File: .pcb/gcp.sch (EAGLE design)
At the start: 14 parts, among them SW1 POWER/COFFEE_SWITCHON-OFF

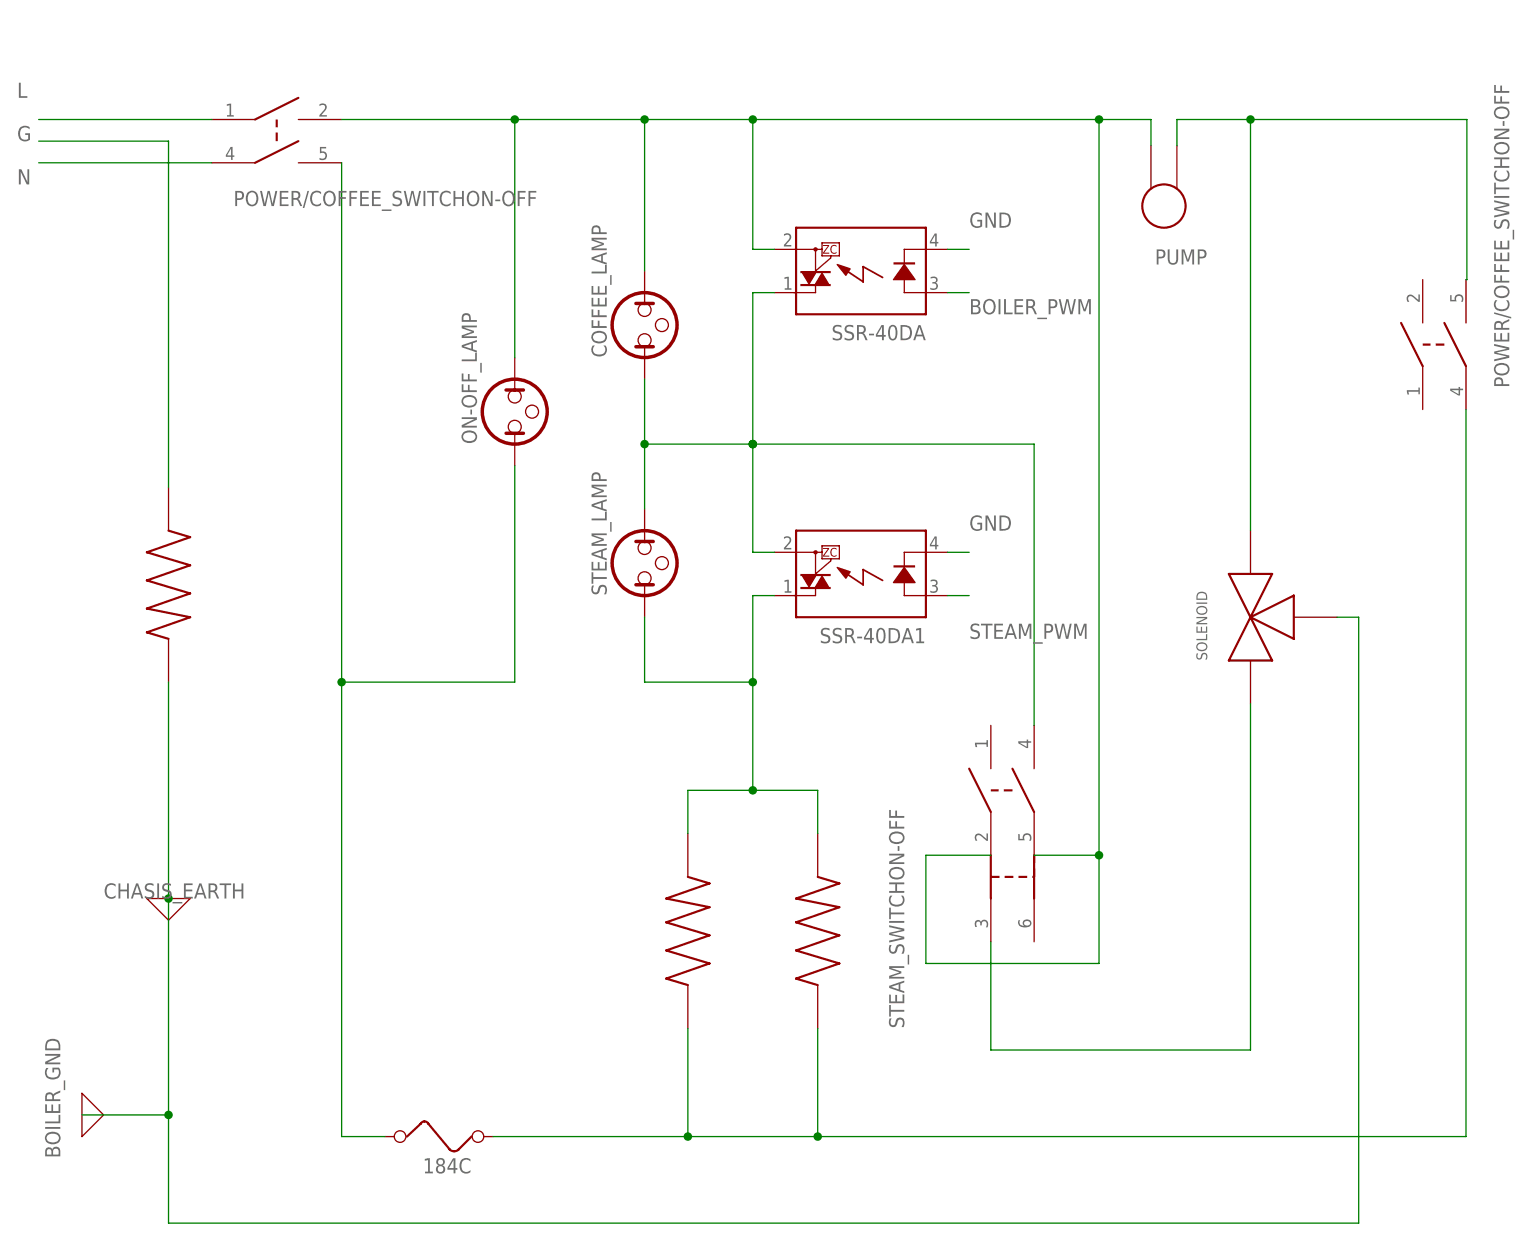
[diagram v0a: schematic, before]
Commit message: Remove references to lights and switches. Updated sketch to reflect how wiring of relays will work (lights will be controlled via physical logic)
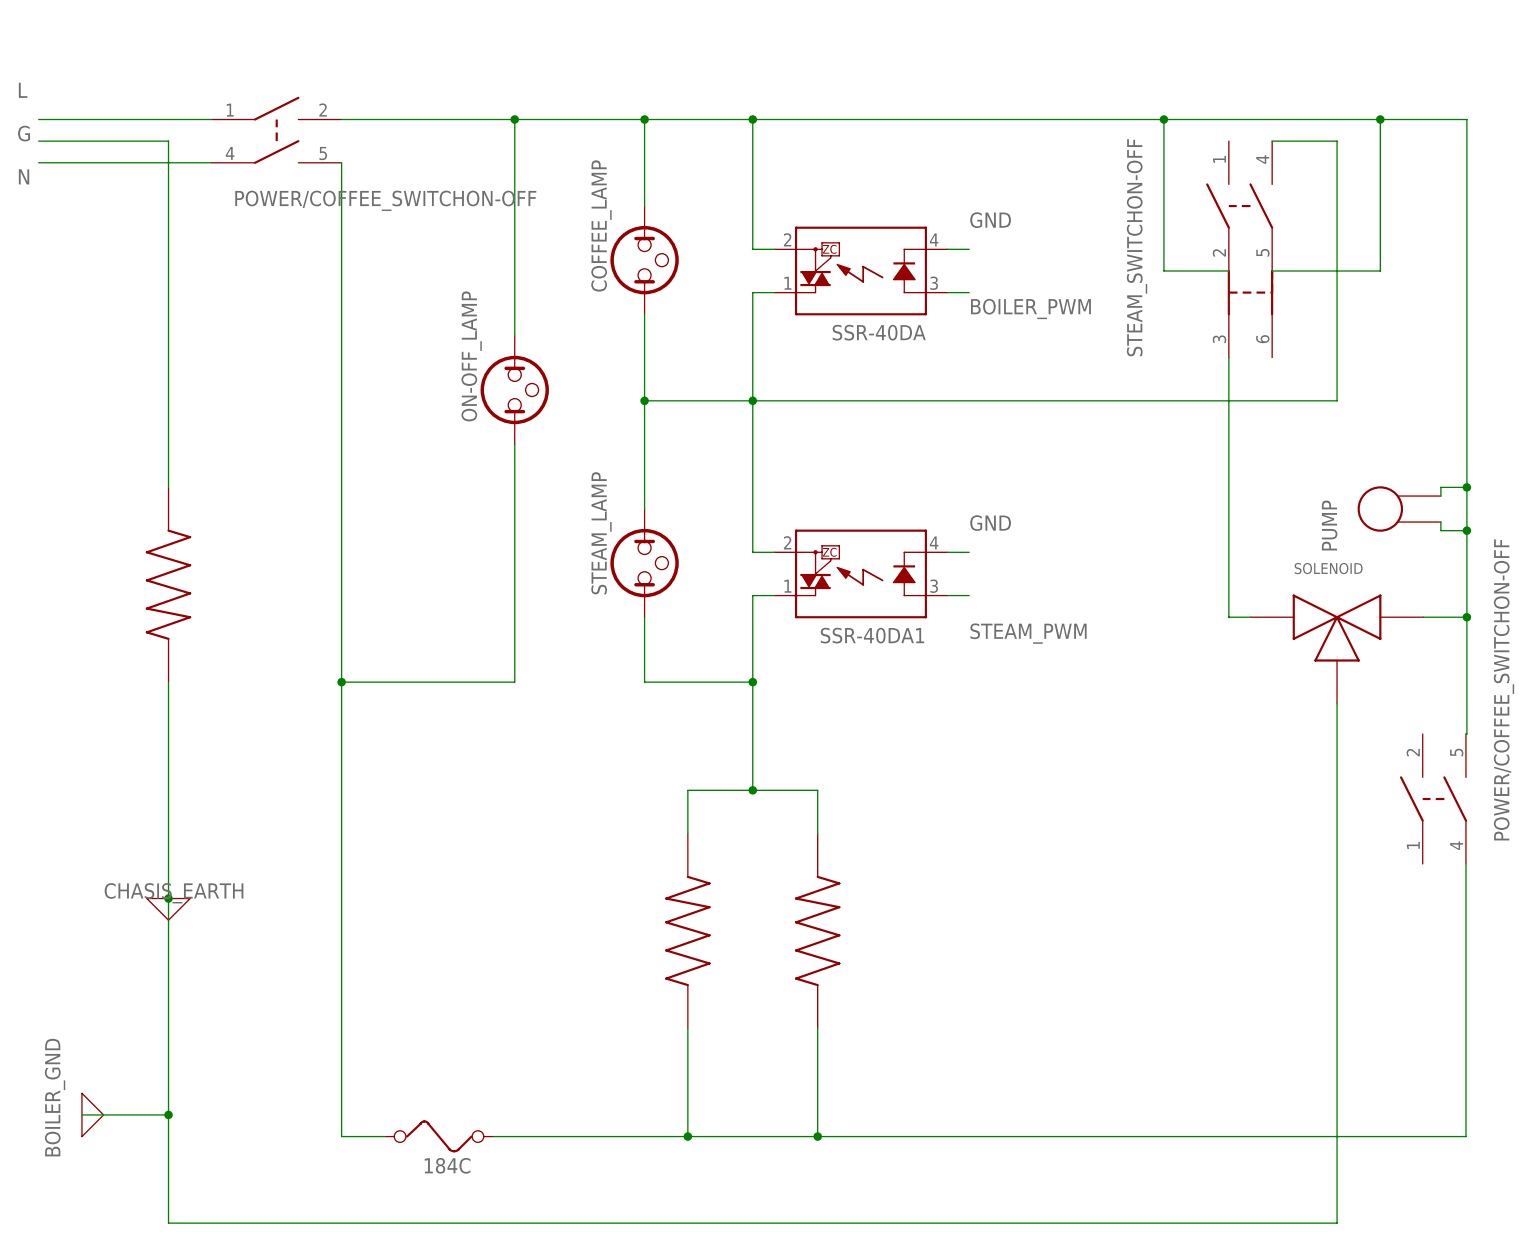
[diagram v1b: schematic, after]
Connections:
- net ORANGE renamed N$1
- removed net N$2: COFFEE_LAMP.2, ON-OFF_LAMP.2, PUMP.P$2, SSR-40DA.DS2, SW1.1, U$4.2, U$4.5
- new net WHITE: COFFEE_LAMP.2, NORMALLY_OPEN.P$2, ON-OFF_LAMP.2, PUMP.P$1, PUMP.P$2, SSR-40DA.DS2, SW1.1, U$3.4, U$4.2, U$4.5
- net GREY: no longer NORMALLY_OPEN.P$2, PUMP.P$1, U$3.4
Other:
- moved on the sheet: COFFEE_LAMP, ON-OFF_LAMP, PUMP

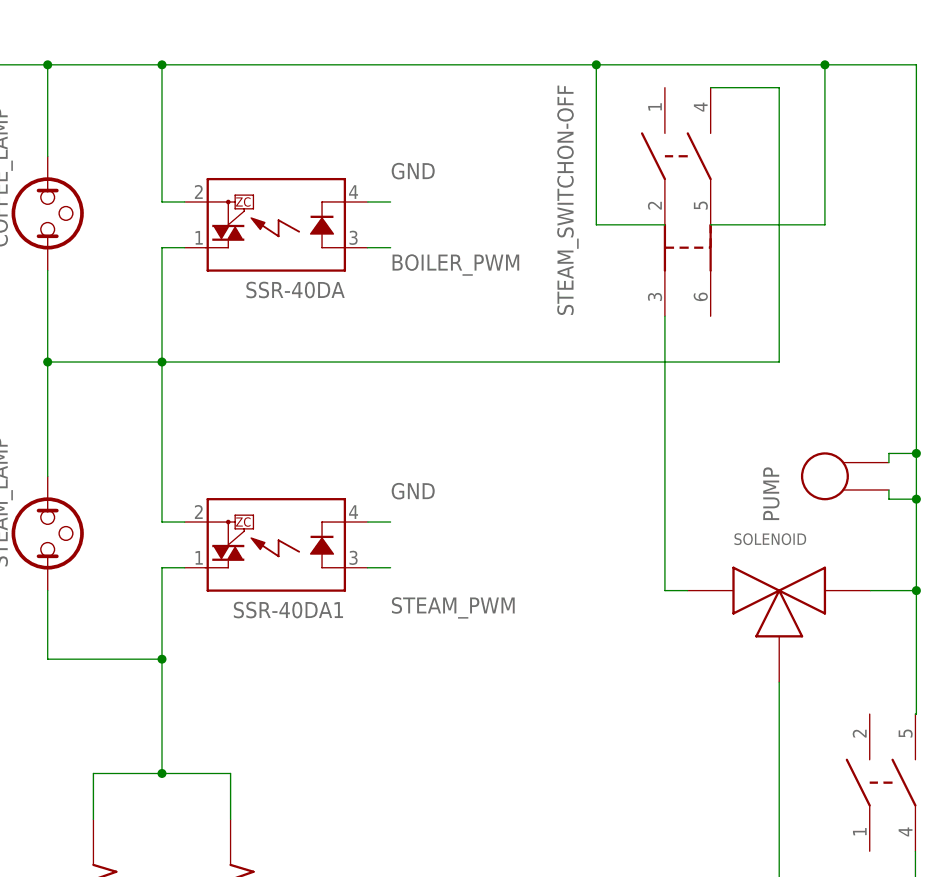
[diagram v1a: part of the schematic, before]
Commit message: Move position of steam relay to allow full manual control.
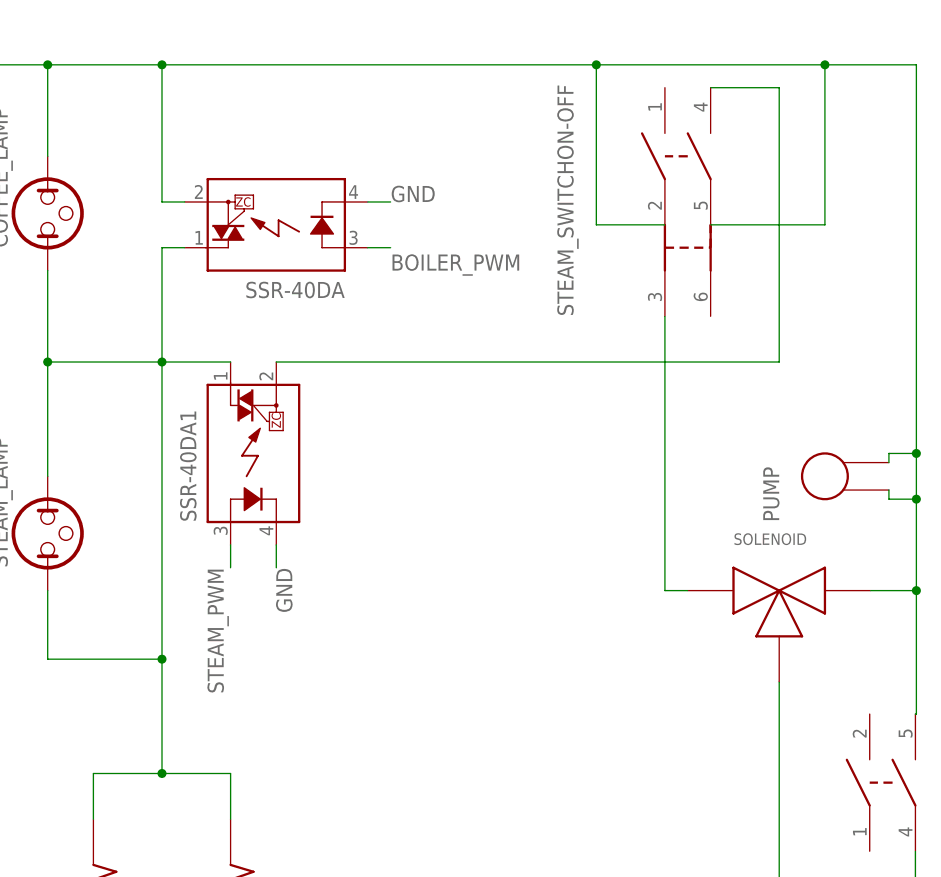
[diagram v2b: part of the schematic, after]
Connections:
- removed net N$4: COFFEE_LAMP.1, SSR-40DA.DS1, SSR-40DA1.DS2, STEAM_LAMP.2, U$4.4
- new net N$2: SSR-40DA1.DS2, U$4.4
- net GREY: now also COFFEE_LAMP.1, SSR-40DA.DS1, STEAM_LAMP.2
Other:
- moved on the sheet: SSR-40DA1
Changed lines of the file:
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@@
 <grid distance="0.1" unitdist="inch" unit="inch" style="lines" multiple="1" display="no" altdistance="0.01" altunitdist="inch" altunit="inch"/>
 <layers>
-<layer number="1" name="Top" color="4" fill="1" visible="yes" active="no"/>
-<layer number="16" name="Bottom" color="1" fill="1" visible="yes" active="no"/>
-<layer number="17" name="Pads" color="2" fill="1" visible="yes" active="no"/>
-<layer number="18" name="Vias" color="2" fill="1" visible="yes" active="no"/>
-<layer number="19" name="Unrouted" color="6" fill="1" visible="yes" active="no"/>
-<layer number="20" name="Dimension" color="24" fill="1" visible="yes" active="no"/>
-<layer number="21" name="tPlace" color="16" fill="1" visible="yes" active="no"/>
-<layer number="22" name="bPlace" color="14" fill="1" visible="yes" active="no"/>
-<layer number="23" name="tOrigins" color="15" fill="1" visible="yes" active="no"/>
-<layer number="24" name="bOrigins" color="15" fill="1" visible="yes" active="no"/>
-<layer number="25" name="tNames" color="7" fill="1" visible="yes" active="no"/>
-<layer number="26" name="bNames" color="7" fill="1" visible="yes" active="no"/>
-<layer number="27" name="tValues" color="7" fill="1" visible="yes" active="no"/>
-<layer number="28" name="bValues" color="7" fill="1" visible="yes" active="no"/>
+<layer number="1" name="Top" color="4" fill="1" visible="no" active="no"/>
+<layer number="16" name="Bottom" color="1" fill="1" visible="no" active="no"/>
+<layer number="17" name="Pads" color="2" fill="1" visible="no" active="no"/>
+<layer number="18" name="Vias" color="2" fill="1" visible="no" active="no"/>
+<layer number="19" name="Unrouted" color="6" fill="1" visible="no" active="no"/>
+<layer number="20" name="Dimension" color="24" fill="1" visible="no" active="no"/>
+<layer number="21" name="tPlace" color="16" fill="1" visible="no" active="no"/>
+<layer number="22" name="bPlace" color="14" fill="1" visible="no" active="no"/>
+<layer number="23" name="tOrigins" color="15" fill="1" visible="no" active="no"/>
+<layer number="24" name="bOrigins" color="15" fill="1" visible="no" active="no"/>
+<layer number="25" name="tNames" color="7" fill="1" visible="no" active="no"/>
+<layer number="26" name="bNames" color="7" fill="1" visible="no" active="no"/>
+<layer number="27" name="tValues" color="7" fill="1" visible="no" active="no"/>
+<layer number="28" name="bValues" color="7" fill="1" visible="no" active="no"/>
 <layer number="29" name="tStop" color="7" fill="3" visible="no" active="no"/>
 <layer number="30" name="bStop" color="7" fill="6" visible="no" active="no"/>
@@
 <layer number="35" name="tGlue" color="7" fill="4" visible="no" active="no"/>
 <layer number="36" name="bGlue" color="7" fill="5" visible="no" active="no"/>
-<layer number="37" name="tTest" color="7" fill="1" visible="yes" active="no"/>
-<layer number="38" name="bTest" color="7" fill="1" visible="yes" active="no"/>
+<layer number="37" name="tTest" color="7" fill="1" visible="no" active="no"/>
+<layer number="38" name="bTest" color="7" fill="1" visible="no" active="no"/>
 <layer number="39" name="tKeepout" color="4" fill="11" visible="no" active="no"/>
 <layer number="40" name="bKeepout" color="1" fill="11" visible="no" active="no"/>
@@
 <layer number="44" name="Drills" color="7" fill="1" visible="no" active="no"/>
 <layer number="45" name="Holes" color="7" fill="1" visible="no" active="no"/>
-<layer number="46" name="Milling" color="3" fill="1" visible="yes" active="no"/>
-<layer number="47" name="Measures" color="7" fill="1" visible="yes" active="no"/>
-<layer number="48" name="Document" color="7" fill="1" visible="yes" active="no"/>
-<layer number="49" name="Reference" color="7" fill="1" visible="yes" active="no"/>
-<layer number="50" name="dxf" color="7" fill="1" visible="yes" active="no"/>
-<layer number="51" name="tDocu" color="6" fill="1" visible="yes" active="no"/>
-<layer number="52" name="bDocu" color="7" fill="1" visible="yes" active="no"/>
-<layer number="53" name="tGND_GNDA" color="7" fill="9" visible="yes" active="no"/>
-<layer number="54" name="bGND_GNDA" color="1" fill="9" visible="yes" active="no"/>
-<layer number="56" name="wert" color="7" fill="1" visible="yes" active="no"/>
-<layer number="57" name="tCAD" color="7" fill="1" visible="yes" active="no"/>
-<layer number="59" name="tCarbon" color="7" fill="1" visible="yes" active="no"/>
-<layer number="60" name="bCarbon" color="7" fill="1" visible="yes" active="no"/>
+<layer number="46" name="Milling" color="3" fill="1" visible="no" active="no"/>
+<layer number="47" name="Measures" color="7" fill="1" visible="no" active="no"/>
+<layer number="48" name="Document" color="7" fill="1" visible="no" active="no"/>
+<layer number="49" name="Reference" color="7" fill="1" visible="no" active="no"/>
+<layer number="50" name="dxf" color="7" fill="1" visible="no" active="no"/>
+<layer number="51" name="tDocu" color="6" fill="1" visible="no" active="no"/>
+<layer number="52" name="bDocu" color="7" fill="1" visible="no" active="no"/>
+<layer number="53" name="tGND_GNDA" color="7" fill="9" visible="no" active="no"/>
+<layer number="54" name="bGND_GNDA" color="1" fill="9" visible="no" active="no"/>
+<layer number="56" name="wert" color="7" fill="1" visible="no" active="no"/>
+<layer number="57" name="tCAD" color="7" fill="1" visible="no" active="no"/>
+<layer number="59" name="tCarbon" color="7" fill="1" visible="no" active="no"/>
+<layer number="60" name="bCarbon" color="7" fill="1" visible="no" active="no"/>
 <layer number="88" name="SimResults" color="9" fill="1" visible="yes" active="yes"/>
 <layer number="89" name="SimProbes" color="9" fill="1" visible="yes" active="yes"/>
@@
 <attribute name="VALUE" x="-215.9" y="22.86" size="1.778" layer="96" rot="R90"/>
 </instance>
-<instance part="SSR-40DA1" gate="G$1" x="-248.92" y="-2.54" smashed="yes" rot="R180">
-<attribute name="NAME" x="-241.3" y="-8.89" size="1.778" layer="95" font="vector" rot="R180"/>
+<instance part="SSR-40DA1" gate="G$1" x="-251.46" y="7.62" smashed="yes" rot="R90">
+<attribute name="NAME" x="-257.81" y="0" size="1.778" layer="95" font="vector" rot="R90"/>
 </instance>
 </instances>
@@
 <segment>
 <wire x1="-238.76" y1="35.56" x2="-236.22" y2="35.56" width="0.1524" layer="91"/>
-<label x="-236.22" y="38.1" size="1.778" layer="95"/>
+<label x="-236.22" y="35.56" size="1.778" layer="95"/>
 <pinref part="SSR-40DA" gate="G$1" pin="K"/>
 </segment>
 <segment>
 <pinref part="SSR-40DA1" gate="G$1" pin="K"/>
-<wire x1="-238.76" y1="0" x2="-236.22" y2="0" width="0.1524" layer="91"/>
-<label x="-236.22" y="2.54" size="1.778" layer="95"/>
+<wire x1="-248.92" y1="-2.54" x2="-248.92" y2="-5.08" width="0.1524" layer="91"/>
+<label x="-248.92" y="-5.08" size="1.778" layer="95" rot="R270"/>
 </segment>
 </net>
@@
 <pinref part="STEAM_LAMP" gate="G$1" pin="1"/>
 <wire x1="-274.32" y1="-15.24" x2="-274.32" y2="-7.62" width="0.1524" layer="91"/>
-<wire x1="-261.62" y1="-5.08" x2="-261.62" y2="-15.24" width="0.1524" layer="91"/>
 <pinref part="HEATER2" gate="G$1" pin="P$2"/>
 <wire x1="-261.62" y1="-15.24" x2="-274.32" y2="-15.24" width="0.1524" layer="91"/>
@@
 <junction x="-261.62" y="-15.24"/>
 <junction x="-261.62" y="-27.94"/>
-<pinref part="SSR-40DA1" gate="G$1" pin="DS1"/>
-<wire x1="-261.62" y1="-5.08" x2="-259.08" y2="-5.08" width="0.1524" layer="91"/>
-</segment>
-</net>
-<net name="N$4" class="0">
-<segment>
 <pinref part="SSR-40DA" gate="G$1" pin="DS1"/>
 <wire x1="-259.08" y1="30.48" x2="-261.62" y2="30.48" width="0.1524" layer="91"/>
@@
 <wire x1="-274.32" y1="27.94" x2="-274.32" y2="17.78" width="0.1524" layer="91"/>
 <wire x1="-261.62" y1="30.48" x2="-261.62" y2="17.78" width="0.1524" layer="91"/>
-<pinref part="U$4" gate="G$1" pin="4"/>
-<wire x1="-261.62" y1="17.78" x2="-261.62" y2="0" width="0.1524" layer="91"/>
-<pinref part="SSR-40DA1" gate="G$1" pin="DS2"/>
-<wire x1="-261.62" y1="0" x2="-259.08" y2="0" width="0.1524" layer="91"/>
-<wire x1="-200.66" y1="48.26" x2="-193.04" y2="48.26" width="0.1524" layer="91"/>
-<wire x1="-193.04" y1="48.26" x2="-193.04" y2="17.78" width="0.1524" layer="91"/>
-<wire x1="-193.04" y1="17.78" x2="-261.62" y2="17.78" width="0.1524" layer="91"/>
+<wire x1="-261.62" y1="17.78" x2="-261.62" y2="-15.24" width="0.1524" layer="91"/>
 <junction x="-261.62" y="17.78"/>
 <wire x1="-261.62" y1="17.78" x2="-274.32" y2="17.78" width="0.1524" layer="91"/>
 <junction x="-274.32" y="17.78"/>
+<wire x1="-254" y1="17.78" x2="-261.62" y2="17.78" width="0.1524" layer="91"/>
+<pinref part="SSR-40DA1" gate="G$1" pin="DS1"/>
 </segment>
 </net>
@@
 <segment>
 <pinref part="SSR-40DA1" gate="G$1" pin="A"/>
-<wire x1="-238.76" y1="-5.08" x2="-236.22" y2="-5.08" width="0.1524" layer="91"/>
-<label x="-236.22" y="-10.16" size="1.778" layer="95"/>
+<wire x1="-254" y1="-2.54" x2="-254" y2="-5.08" width="0.1524" layer="91"/>
+<label x="-256.54" y="-5.08" size="1.778" layer="95" rot="R270"/>
 </segment>
 </net>
@@
 </segment>
 </net>
+<net name="N$2" class="0">
+<segment>
+<wire x1="-193.04" y1="17.78" x2="-248.92" y2="17.78" width="0.1524" layer="91"/>
+<pinref part="U$4" gate="G$1" pin="4"/>
+<wire x1="-200.66" y1="48.26" x2="-193.04" y2="48.26" width="0.1524" layer="91"/>
+<wire x1="-193.04" y1="48.26" x2="-193.04" y2="17.78" width="0.1524" layer="91"/>
+<pinref part="SSR-40DA1" gate="G$1" pin="DS2"/>
+</segment>
+</net>
